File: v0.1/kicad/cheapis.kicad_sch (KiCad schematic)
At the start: 25 parts, among them J1 Conn_01x01, SW1 SW_Diode_Combined, SW10 SW_Diode_Combined, SW11 SW_Diode_Combined, SW12 SW_Diode_Combined, SW13 SW_Diode_Combined, SW14 SW_Diode_Combined, SW15 SW_Diode_Combined, SW16 SW_Diode_Combined, SW17 SW_Diode_Combined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

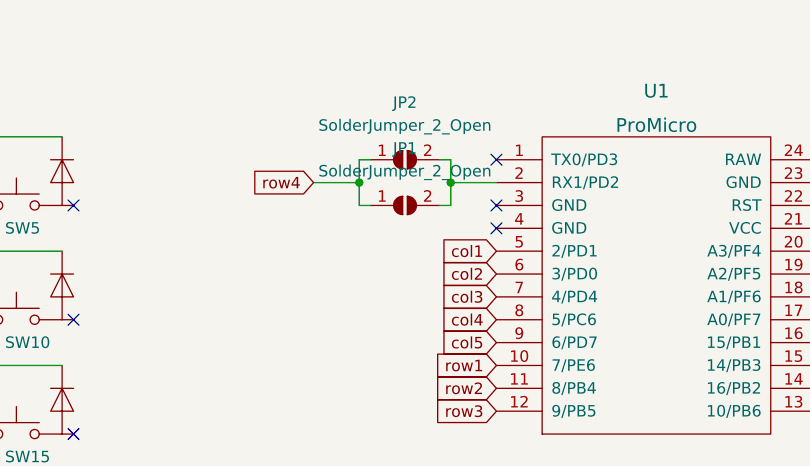
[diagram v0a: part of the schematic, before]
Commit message: add customized SW_Redragon_LowProfile_1.00u footprint
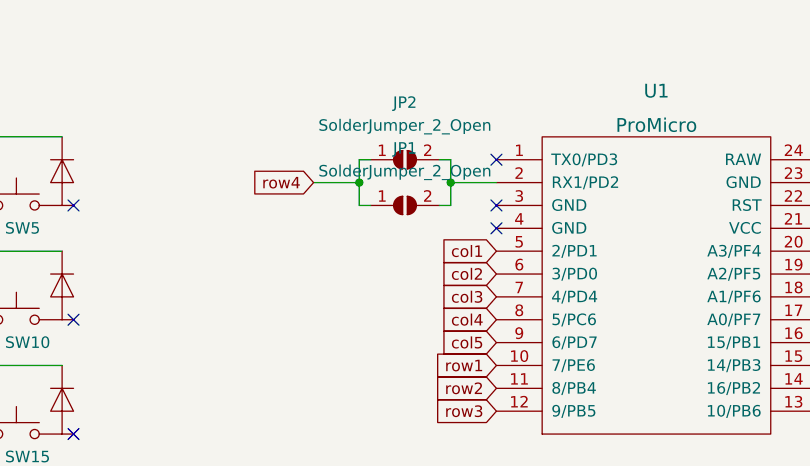
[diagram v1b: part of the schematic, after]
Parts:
- SW1: footprint dotleon:SW_MX_GATLP_CHOC_reversible -> Redragon:SW_Redragon_LowProfile_PCB_1.00u

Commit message: first prototype design
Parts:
- SW10, SW12, SW13, SW14, SW15, SW16, SW17, SW2, SW3, SW4, SW5, SW6, SW7, SW8, SW9: footprint dotleon:SW_MX_GATLP_CHOC_reversible -> Redragon:SW_Redragon_LowProfile_PCB_1.00u
- SW11: footprint dotleon:SW_MX_GATLP_CHOC_reversible_sideofpcb -> Redragon:SW_Redragon_LowProfile_PCB_1.00u
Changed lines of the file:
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@@
 			)
 		)
-		(property "Footprint" "dotleon:SW_MX_GATLP_CHOC_reversible"
+		(property "Footprint" "Redragon:SW_Redragon_LowProfile_PCB_1.00u"
 			(at 100.33 59.69 0)
 			(effects
@@
 			)
 		)
-		(property "Footprint" "dotleon:SW_MX_GATLP_CHOC_reversible"
+		(property "Footprint" "Redragon:SW_Redragon_LowProfile_PCB_1.00u"
 			(at 100.33 46.99 0)
 			(effects
@@
 			)
 		)
-		(property "Footprint" "dotleon:SW_MX_GATLP_CHOC_reversible"
+		(property "Footprint" "Redragon:SW_Redragon_LowProfile_PCB_1.00u"
 			(at 69.85 72.39 0)
 			(effects
@@
 			)
 		)
-		(property "Footprint" "dotleon:SW_MX_GATLP_CHOC_reversible"
+		(property "Footprint" "Redragon:SW_Redragon_LowProfile_PCB_1.00u"
 			(at 115.57 72.39 0)
 			(effects
@@
 			)
 		)
-		(property "Footprint" "dotleon:SW_MX_GATLP_CHOC_reversible"
+		(property "Footprint" "Redragon:SW_Redragon_LowProfile_PCB_1.00u"
 			(at 100.33 85.09 0)
 			(effects
@@
 			)
 		)
-		(property "Footprint" "dotleon:SW_MX_GATLP_CHOC_reversible"
+		(property "Footprint" "Redragon:SW_Redragon_LowProfile_PCB_1.00u"
 			(at 85.09 72.39 0)
 			(effects
@@
 			)
 		)
-		(property "Footprint" "dotleon:SW_MX_GATLP_CHOC_reversible"
+		(property "Footprint" "Redragon:SW_Redragon_LowProfile_PCB_1.00u"
 			(at 85.09 46.99 0)
 			(effects
@@
 			)
 		)
-		(property "Footprint" "dotleon:SW_MX_GATLP_CHOC_reversible"
+		(property "Footprint" "Redragon:SW_Redragon_LowProfile_PCB_1.00u"
 			(at 69.85 46.99 0)
 			(effects
@@
 			)
 		)
-		(property "Footprint" "dotleon:SW_MX_GATLP_CHOC_reversible"
+		(property "Footprint" "Redragon:SW_Redragon_LowProfile_PCB_1.00u"
 			(at 100.33 72.39 0)
 			(effects
@@
 			)
 		)
-		(property "Footprint" "dotleon:SW_MX_GATLP_CHOC_reversible_sideofpcb"
+		(property "Footprint" "Redragon:SW_Redragon_LowProfile_PCB_1.00u"
 			(at 54.61 72.39 0)
 			(effects
@@
 			)
 		)
-		(property "Footprint" "dotleon:SW_MX_GATLP_CHOC_reversible"
+		(property "Footprint" "Redragon:SW_Redragon_LowProfile_PCB_1.00u"
 			(at 115.57 59.69 0)
 			(effects
@@
 			)
 		)
-		(property "Footprint" "dotleon:SW_MX_GATLP_CHOC_reversible"
+		(property "Footprint" "Redragon:SW_Redragon_LowProfile_PCB_1.00u"
 			(at 115.57 46.99 0)
 			(effects
@@
 			)
 		)
-		(property "Footprint" "dotleon:SW_MX_GATLP_CHOC_reversible"
+		(property "Footprint" "Redragon:SW_Redragon_LowProfile_PCB_1.00u"
 			(at 115.57 85.09 0)
 			(effects
@@
 			)
 		)
-		(property "Footprint" "dotleon:SW_MX_GATLP_CHOC_reversible"
+		(property "Footprint" "Redragon:SW_Redragon_LowProfile_PCB_1.00u"
 			(at 85.09 59.69 0)
 			(effects
@@
 			)
 		)
-		(property "Footprint" "dotleon:SW_MX_GATLP_CHOC_reversible"
+		(property "Footprint" "Redragon:SW_Redragon_LowProfile_PCB_1.00u"
 			(at 69.85 59.69 0)
 			(effects
@@
 			)
 		)
-		(property "Footprint" "dotleon:SW_MX_GATLP_CHOC_reversible"
+		(property "Footprint" "Redragon:SW_Redragon_LowProfile_PCB_1.00u"
 			(at 54.61 59.69 0)
 			(effects

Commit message: multi-switches-support
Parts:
- SW1, SW10, SW11, SW12, SW13, SW14, SW15, SW16, SW17, SW2, SW3, SW4, SW5, SW6, SW7, SW8, SW9: footprint Redragon:SW_Redragon_LowProfile_PCB_1.00u -> Redragon:MultiSwitches_MX_Redragon_ChocV1
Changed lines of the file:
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@@
 			)
 		)
-		(property "Footprint" "Redragon:SW_Redragon_LowProfile_PCB_1.00u"
+		(property "Footprint" "Redragon:MultiSwitches_MX_Redragon_ChocV1"
 			(at 100.33 59.69 0)
 			(effects
@@
 			)
 		)
-		(property "Footprint" "Redragon:SW_Redragon_LowProfile_PCB_1.00u"
+		(property "Footprint" "Redragon:MultiSwitches_MX_Redragon_ChocV1"
 			(at 54.61 46.99 0)
 			(effects
@@
 			)
 		)
-		(property "Footprint" "Redragon:SW_Redragon_LowProfile_PCB_1.00u"
+		(property "Footprint" "Redragon:MultiSwitches_MX_Redragon_ChocV1"
 			(at 100.33 46.99 0)
 			(effects
@@
 			)
 		)
-		(property "Footprint" "Redragon:SW_Redragon_LowProfile_PCB_1.00u"
+		(property "Footprint" "Redragon:MultiSwitches_MX_Redragon_ChocV1"
 			(at 69.85 72.39 0)
 			(effects
@@
 			)
 		)
-		(property "Footprint" "Redragon:SW_Redragon_LowProfile_PCB_1.00u"
+		(property "Footprint" "Redragon:MultiSwitches_MX_Redragon_ChocV1"
 			(at 115.57 72.39 0)
 			(effects
@@
 			)
 		)
-		(property "Footprint" "Redragon:SW_Redragon_LowProfile_PCB_1.00u"
+		(property "Footprint" "Redragon:MultiSwitches_MX_Redragon_ChocV1"
 			(at 100.33 85.09 0)
 			(effects
@@
 			)
 		)
-		(property "Footprint" "Redragon:SW_Redragon_LowProfile_PCB_1.00u"
+		(property "Footprint" "Redragon:MultiSwitches_MX_Redragon_ChocV1"
 			(at 85.09 72.39 0)
 			(effects
@@
 			)
 		)
-		(property "Footprint" "Redragon:SW_Redragon_LowProfile_PCB_1.00u"
+		(property "Footprint" "Redragon:MultiSwitches_MX_Redragon_ChocV1"
 			(at 85.09 46.99 0)
 			(effects
@@
 			)
 		)
-		(property "Footprint" "Redragon:SW_Redragon_LowProfile_PCB_1.00u"
+		(property "Footprint" "Redragon:MultiSwitches_MX_Redragon_ChocV1"
 			(at 69.85 46.99 0)
 			(effects
@@
 			)
 		)
-		(property "Footprint" "Redragon:SW_Redragon_LowProfile_PCB_1.00u"
+		(property "Footprint" "Redragon:MultiSwitches_MX_Redragon_ChocV1"
 			(at 100.33 72.39 0)
 			(effects
@@
 			)
 		)
-		(property "Footprint" "Redragon:SW_Redragon_LowProfile_PCB_1.00u"
+		(property "Footprint" "Redragon:MultiSwitches_MX_Redragon_ChocV1"
 			(at 54.61 72.39 0)
 			(effects
@@
 			)
 		)
-		(property "Footprint" "Redragon:SW_Redragon_LowProfile_PCB_1.00u"
+		(property "Footprint" "Redragon:MultiSwitches_MX_Redragon_ChocV1"
 			(at 115.57 59.69 0)
 			(effects
@@
 			)
 		)
-		(property "Footprint" "Redragon:SW_Redragon_LowProfile_PCB_1.00u"
+		(property "Footprint" "Redragon:MultiSwitches_MX_Redragon_ChocV1"
 			(at 115.57 46.99 0)
 			(effects
@@
 			)
 		)
-		(property "Footprint" "Redragon:SW_Redragon_LowProfile_PCB_1.00u"
+		(property "Footprint" "Redragon:MultiSwitches_MX_Redragon_ChocV1"
 			(at 115.57 85.09 0)
 			(effects
@@
 			)
 		)
-		(property "Footprint" "Redragon:SW_Redragon_LowProfile_PCB_1.00u"
+		(property "Footprint" "Redragon:MultiSwitches_MX_Redragon_ChocV1"
 			(at 85.09 59.69 0)
 			(effects
@@
 			)
 		)
-		(property "Footprint" "Redragon:SW_Redragon_LowProfile_PCB_1.00u"
+		(property "Footprint" "Redragon:MultiSwitches_MX_Redragon_ChocV1"
 			(at 69.85 59.69 0)
 			(effects
@@
 			)
 		)
-		(property "Footprint" "Redragon:SW_Redragon_LowProfile_PCB_1.00u"
+		(property "Footprint" "Redragon:MultiSwitches_MX_Redragon_ChocV1"
 			(at 54.61 59.69 0)
 			(effects
